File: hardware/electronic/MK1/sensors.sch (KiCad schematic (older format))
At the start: 5 parts

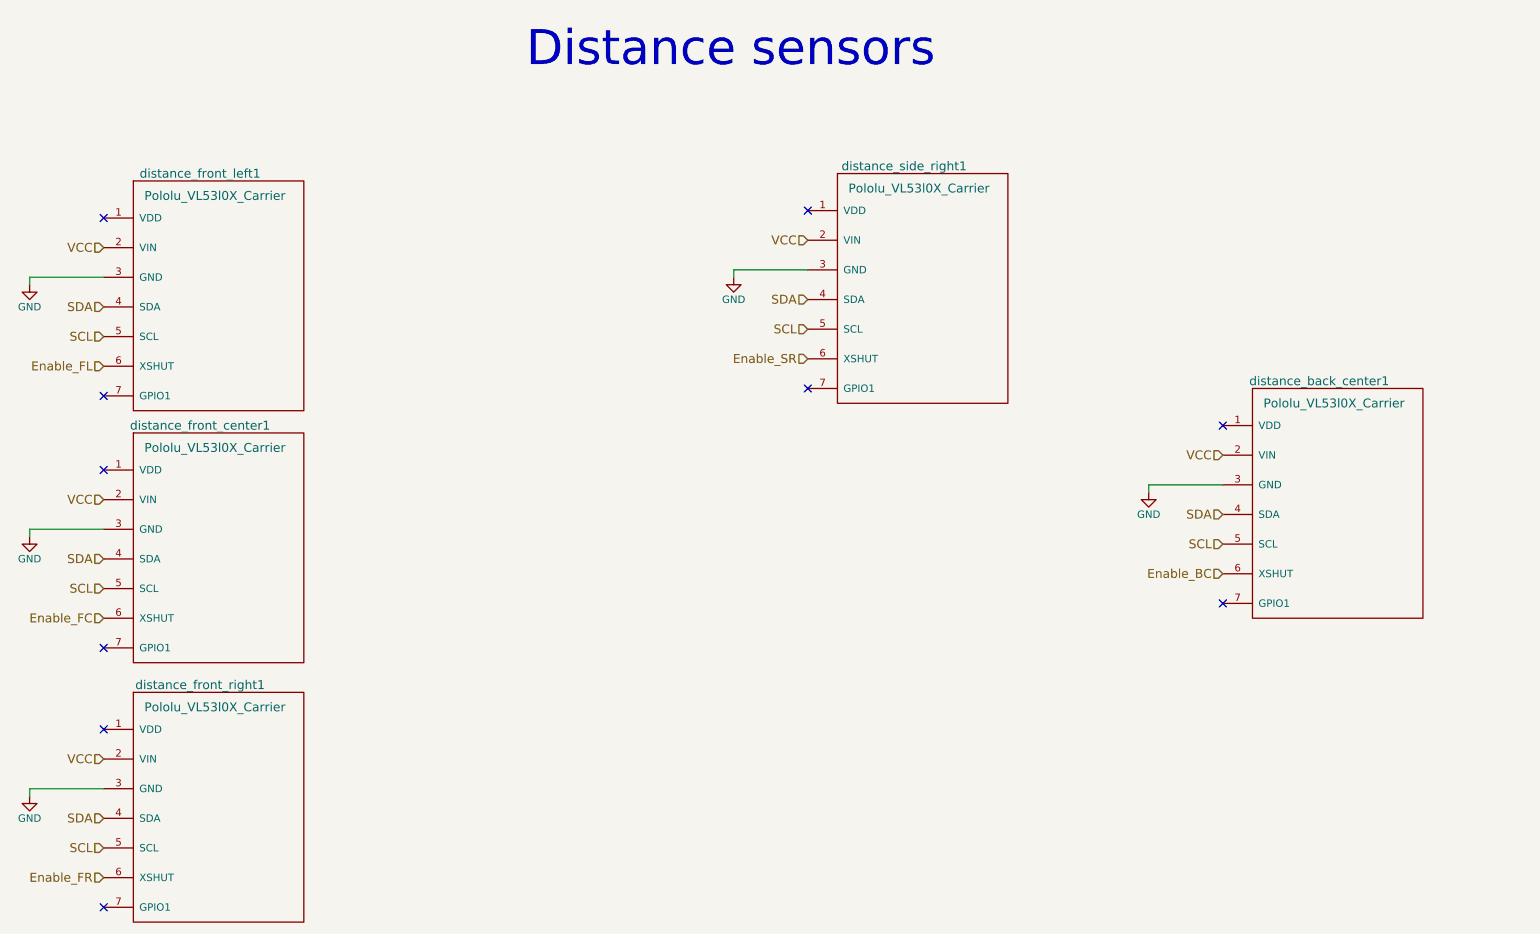
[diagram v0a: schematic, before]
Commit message: HW: Add missing component values
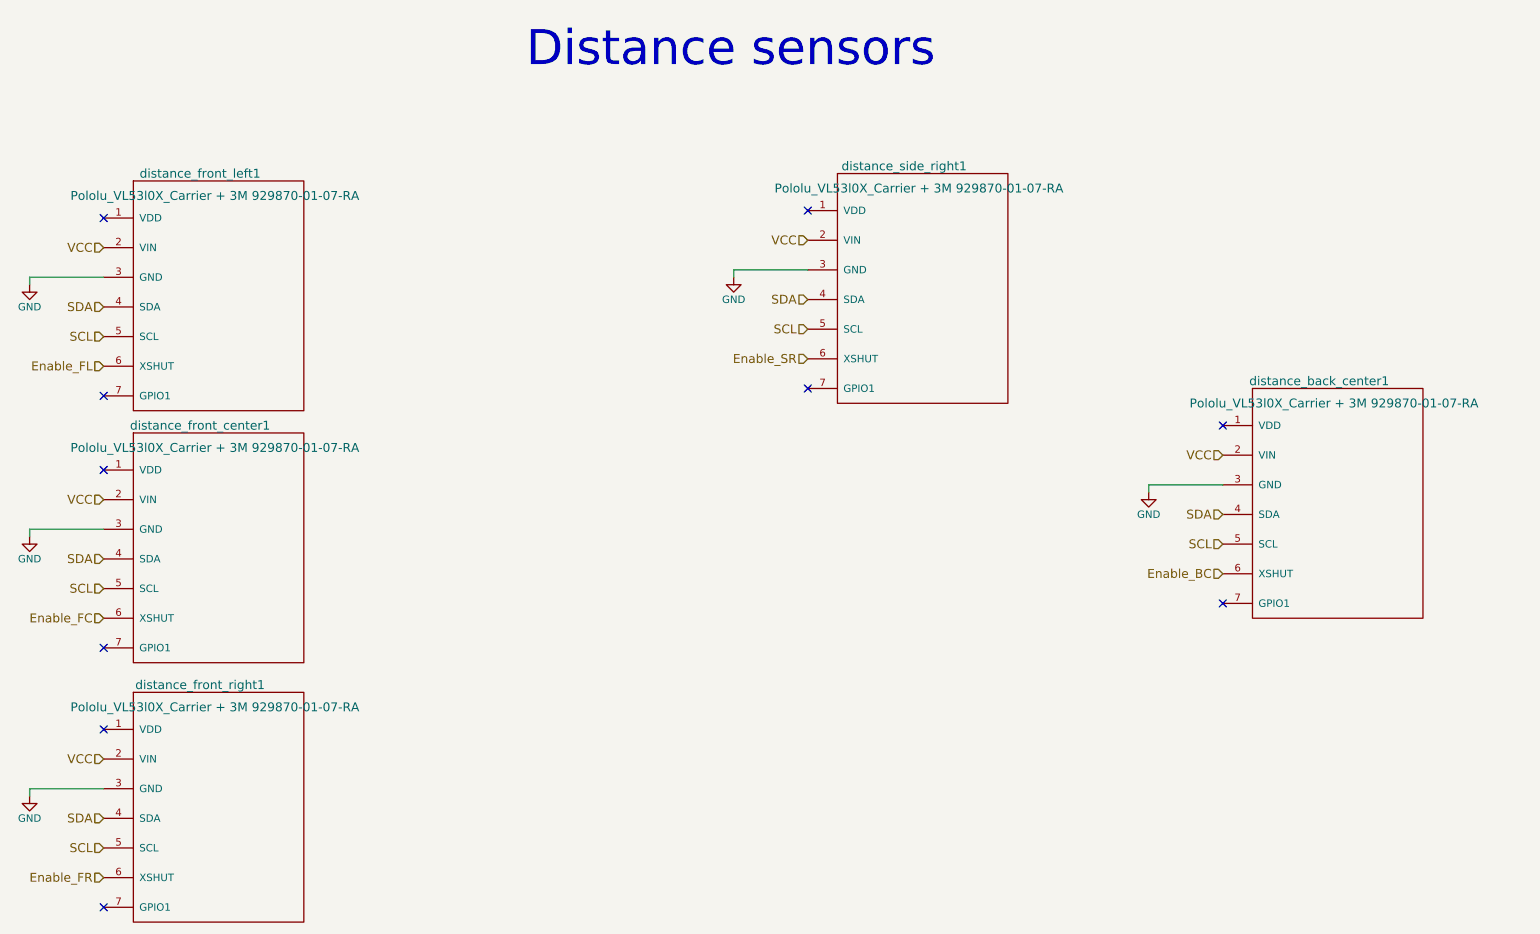
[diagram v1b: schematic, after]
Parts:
- distance_back_center1, distance_front_center1, distance_front_left1, distance_front_right1, distance_side_right1: value Pololu_VL53l0X_Carrier -> Pololu_VL53l0X_Carrier + 3M 929870-01-07-RA
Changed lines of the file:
@@
 P 1750 3400
 F 0 "distance_front_center1" H 2200 3450 60  0000 C CNN
-F 1 "Pololu_VL53l0X_Carrier" H 2300 3300 60  0000 C CNN
+F 1 "Pololu_VL53l0X_Carrier + 3M 929870-01-07-RA" H 2300 3300 60  0000 C CNN
 F 2 "OPAVES_Footprints:Pololu_VL53L0x_Carrier" H 1750 3350 60  0001 C CNN
 F 3 "" H 1750 3350 60  0001 C CNN
@@
 P 1750 5150
 F 0 "distance_front_right1" H 2200 5200 60  0000 C CNN
-F 1 "Pololu_VL53l0X_Carrier" H 2300 5050 60  0000 C CNN
+F 1 "Pololu_VL53l0X_Carrier + 3M 929870-01-07-RA" H 2300 5050 60  0000 C CNN
 F 2 "OPAVES_Footprints:Pololu_VL53L0x_Carrier" H 1750 5100 60  0001 C CNN
 F 3 "" H 1750 5100 60  0001 C CNN
@@
 P 1750 1700
 F 0 "distance_front_left1" H 2200 1750 60  0000 C CNN
-F 1 "Pololu_VL53l0X_Carrier" H 2300 1600 60  0000 C CNN
+F 1 "Pololu_VL53l0X_Carrier + 3M 929870-01-07-RA" H 2300 1600 60  0000 C CNN
 F 2 "OPAVES_Footprints:Pololu_VL53L0x_Carrier" H 1750 1650 60  0001 C CNN
 F 3 "" H 1750 1650 60  0001 C CNN
@@
 P 9300 3100
 F 0 "distance_back_center1" H 9750 3150 60  0000 C CNN
-F 1 "Pololu_VL53l0X_Carrier" H 9850 3000 60  0000 C CNN
+F 1 "Pololu_VL53l0X_Carrier + 3M 929870-01-07-RA" H 9850 3000 60  0000 C CNN
 F 2 "OPAVES_Footprints:Pololu_VL53L0x_Carrier" H 9300 3050 60  0001 C CNN
 F 3 "" H 9300 3050 60  0001 C CNN
@@
 P 6500 1650
 F 0 "distance_side_right1" H 6950 1700 60  0000 C CNN
-F 1 "Pololu_VL53l0X_Carrier" H 7050 1550 60  0000 C CNN
+F 1 "Pololu_VL53l0X_Carrier + 3M 929870-01-07-RA" H 7050 1550 60  0000 C CNN
 F 2 "OPAVES_Footprints:Pololu_VL53L0x_Carrier" H 6500 1600 60  0001 C CNN
 F 3 "" H 6500 1600 60  0001 C CNN
